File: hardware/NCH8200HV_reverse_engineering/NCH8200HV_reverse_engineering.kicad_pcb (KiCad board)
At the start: 2 copper layers, 26.3 x 19.9 mm, 19 parts, among them Q1 CSD17573Q5BT, U1 MAX668EUB

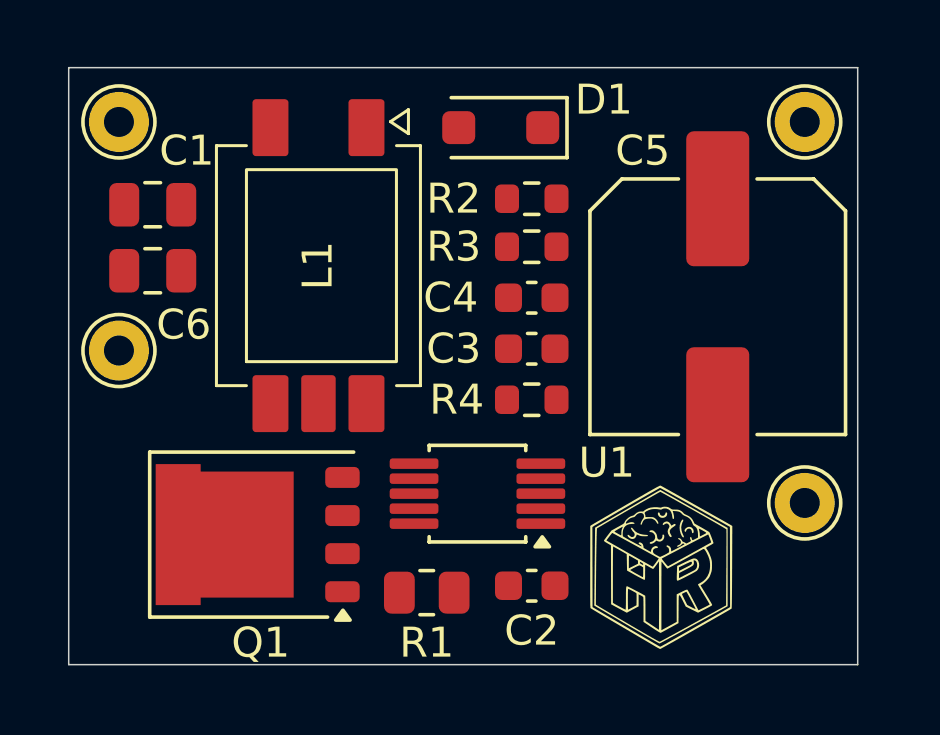
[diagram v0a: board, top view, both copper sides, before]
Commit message: hardware(pcb): modify layout
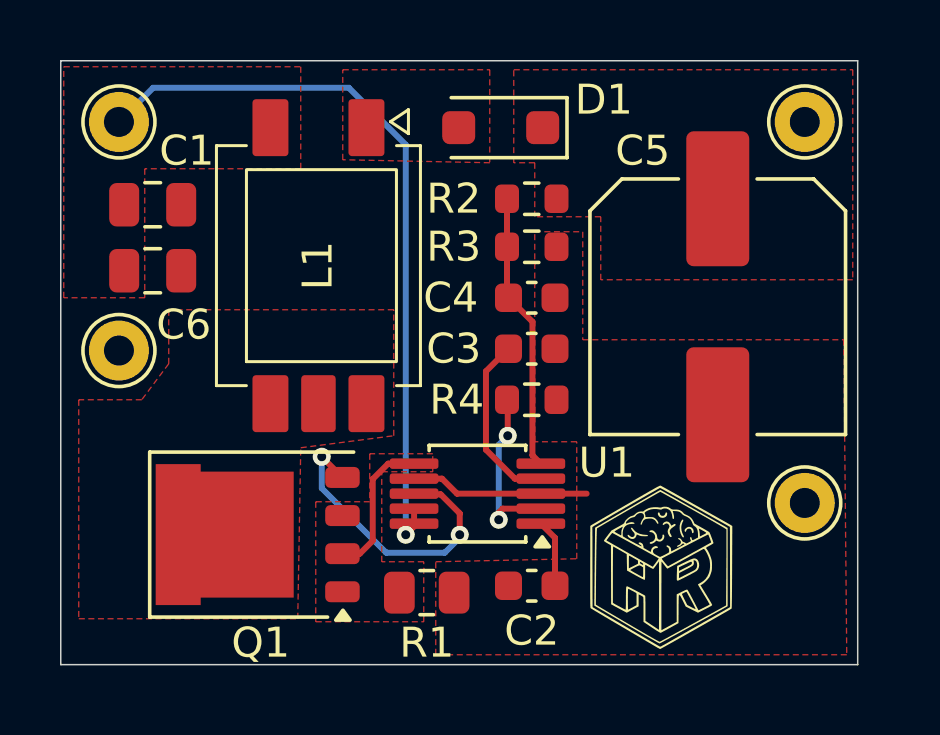
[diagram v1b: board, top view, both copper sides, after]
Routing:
- net Vin: track 0.00 -> 24.8 mm, vias 0 -> 1
- net Net-(Q1-G): track 0.00 -> 10.3 mm, vias 0 -> 2
- net Vfb: track 0.00 -> 9.30 mm
- net GND: track 0.00 -> 5.96 mm
- net Net-(U1-REF): track 0.00 -> 5.90 mm
- net Net-(U1-FREQ): track 0.00 -> 5.83 mm, vias 0 -> 2
- net Net-(Q1-S): track 0.00 -> 4.84 mm
- net Net-(U1-LDO): track 0.00 -> 2.27 mm
- added copper zone on F.Cu, net GND
- added copper zone on F.Cu, net Net-(D1-A)
- added copper zone on F.Cu, net Net-(Q1-D)
- added copper zone on F.Cu, net Net-(Q1-S)
- added copper zone on F.Cu, net Vin
- added copper zone on F.Cu, net Vout
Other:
- board size 26.3 x 19.9 mm -> 26.6 x 20.1 mm

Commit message: hardware(pcb): update NCH8200 reverse engineering pcb
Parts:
- G***: moved to B.Cu
- moved G*** 10.2 mm to (140.9, 98.5), turned to 180 degrees
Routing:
- net Vin: track 24.8 -> 19.4 mm, vias 1 -> 6
- net Net-(Q1-S): track 4.84 -> 5.53 mm
- net Vout: vias 0 -> 4
- net GND: vias 0 -> 8
- added copper zone on B.Cu, net GND
- added copper zone on B.Cu, net Vin
- added copper zone on B.Cu, net Vout
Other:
- board text added: "GND"
- board text added: "MAX668 self-tapped boost converter V0.9.0"
- board text added: "VIN"
- board text added: "VIN 5-12V VOUT 173V"
- board text added: "VOUT"
